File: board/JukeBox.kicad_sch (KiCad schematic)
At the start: 70 parts, among them J1 USB_B_Micro, J2 Conn_01x03, J3 Conn_01x04, J4 Conn_01x08, J5 Conn_01x01, J6 Conn_01x03, J7 Conn_01x03, SW1 SW_SPST, SW10 SW_SPST, SW11 SW_SPST, SW12 SW_SPST, SW2 SW_SPST, SW3 SW_SPST, SW4 SW_SPST, SW5 SW_SPST, SW6 SW_SPST, SW7 SW_SPST, SW8 SW_SPST, SW9 SW_SPST, U1 NCP1117-3.3_SOT223, U2 W25Q128JVS, U3 RP2040, Y1 ABLS-12.000MHZ-B4-T

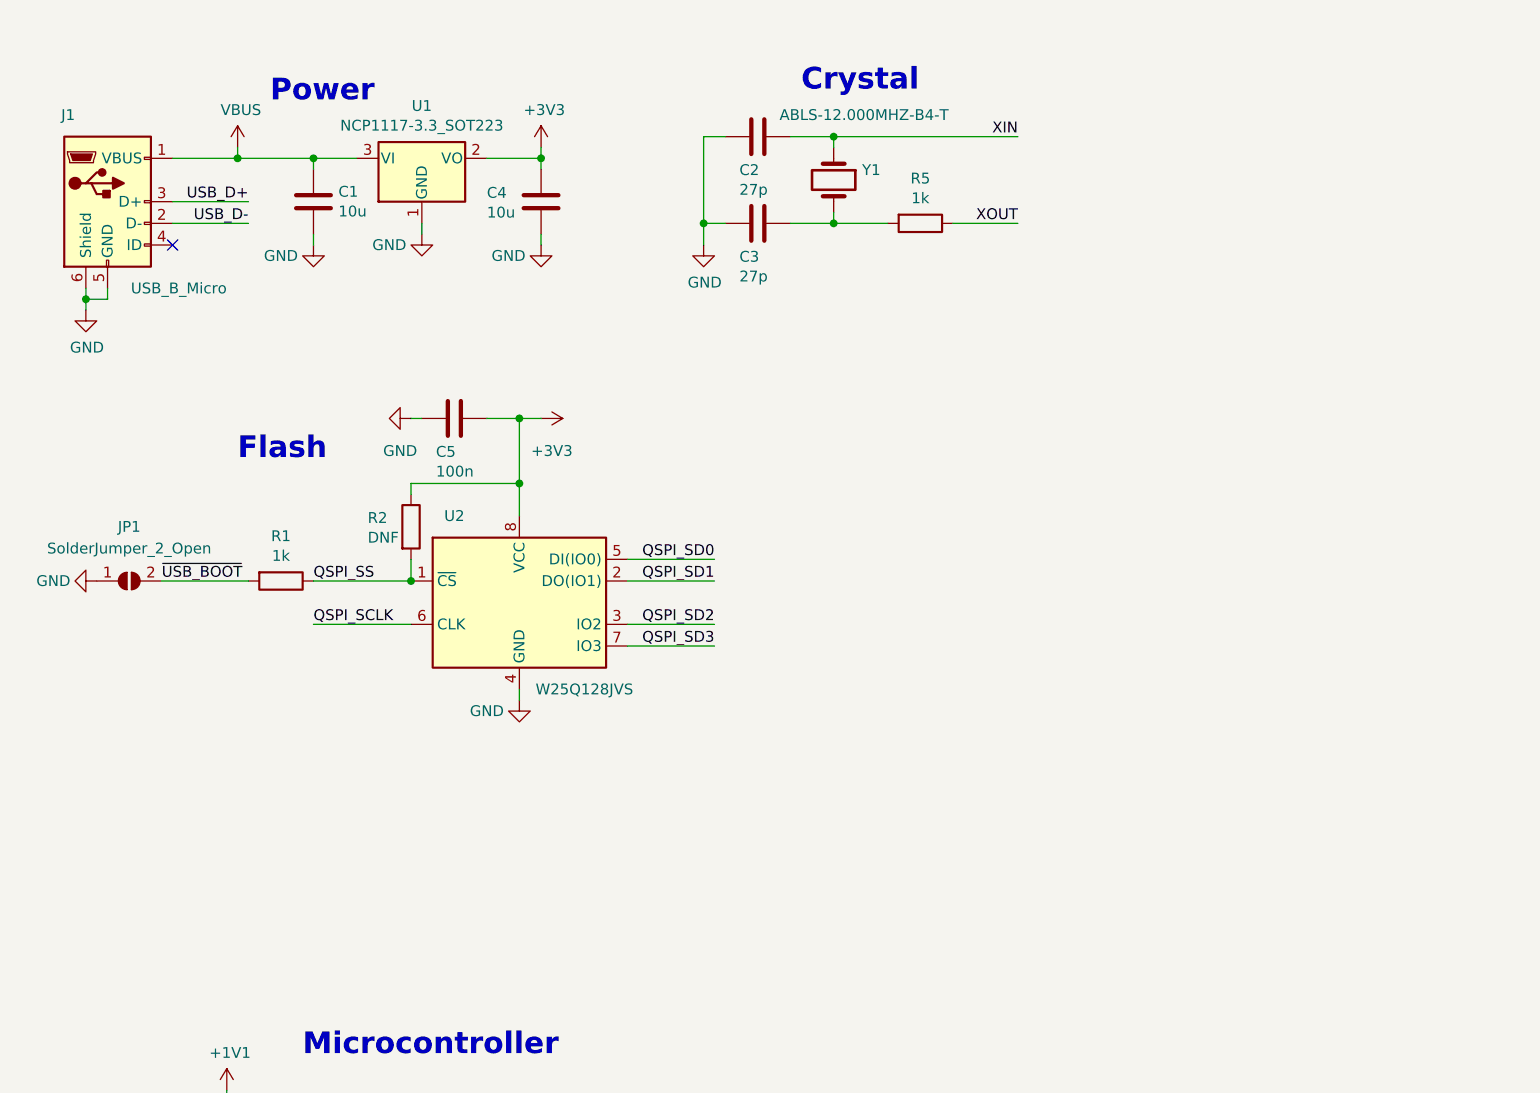
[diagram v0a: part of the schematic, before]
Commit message: add some new footprints and 3d models
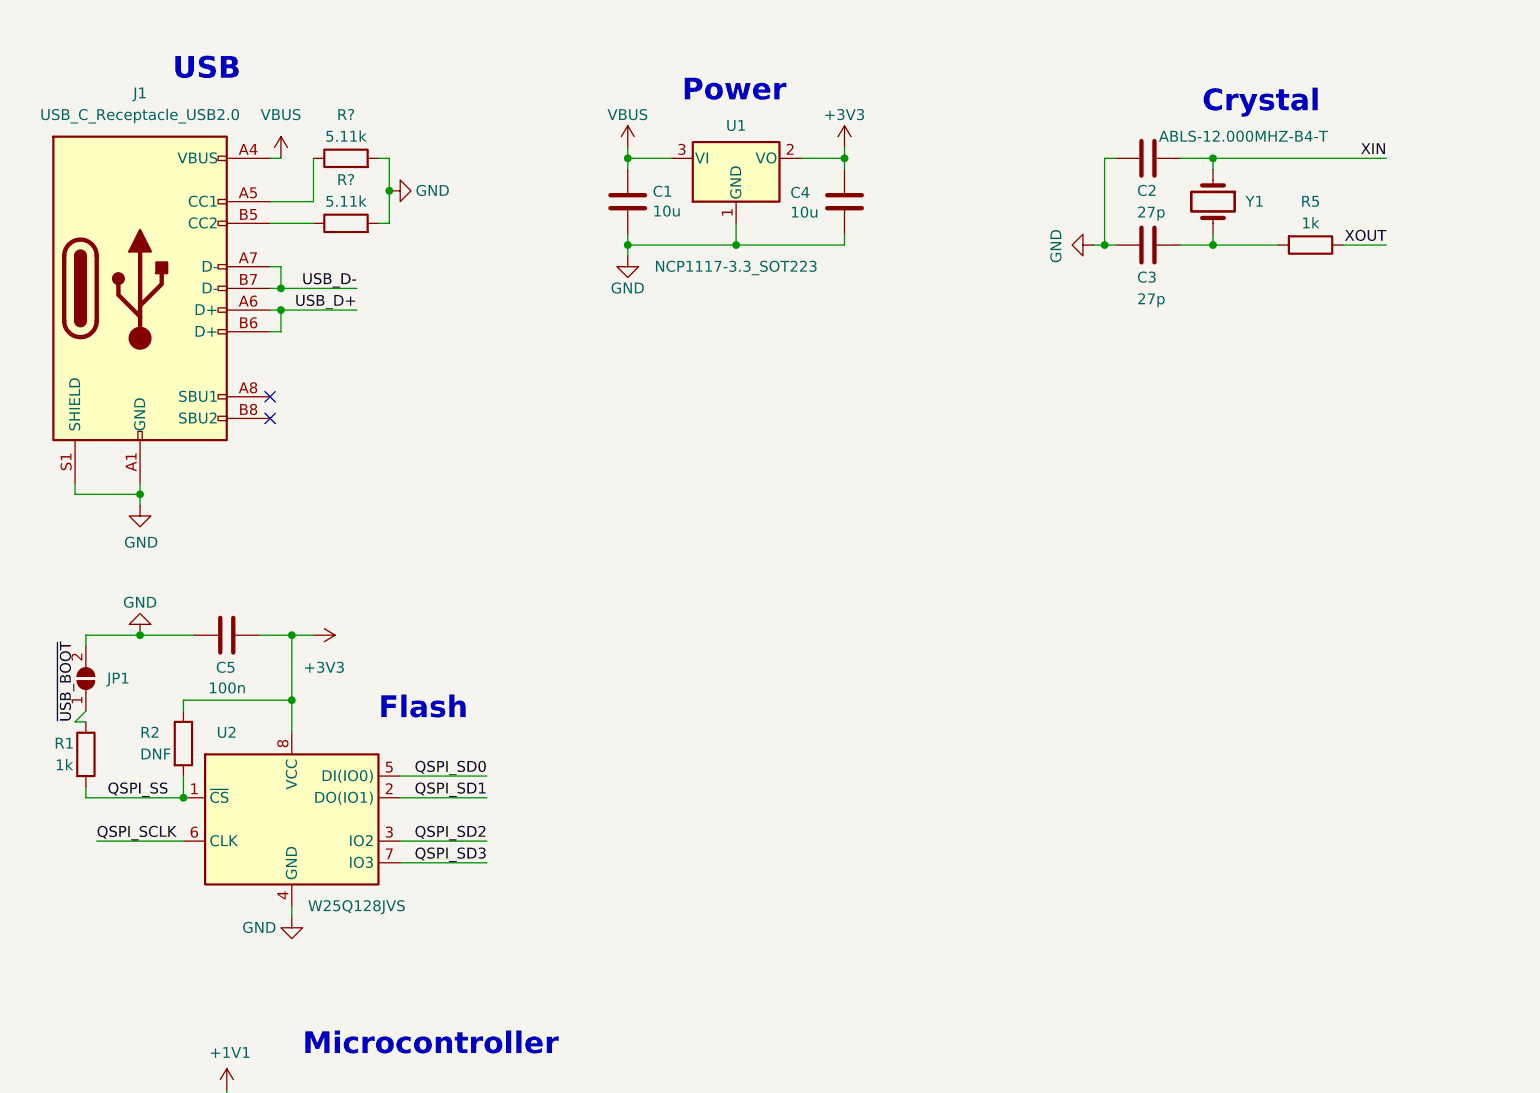
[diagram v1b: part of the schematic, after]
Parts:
- removed J1: USB_B_Micro, RP2040_minimal:USB_Micro-B_Amphenol_10103594-0001LF_Horizontal_modified, symbol Connector:USB_B_Micro
- added J1: USB_C_Receptacle_USB2.0, symbol Connector:USB_C_Receptacle_USB2.0
- added R? (x2): 5.11k, Resistor_SMD:R_1206_3216Metric_Pad1.30x1.75mm_HandSolder, symbol Device:R
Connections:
- net GND: now also JP1.2 (B), J1.A1 (GND), J1.A12 (GND), J1.B1 (GND), J1.B12 (GND), J1.S1 (SHIELD), R?.2, R?.2; no longer JP1.1 (A)
- net QSPI_SS: now also R1.2; no longer R1.1
- net USB_D+: now also J1.A6 (D+), J1.B6 (D+)
- net USB_D-: now also J1.A7 (D-), J1.B7 (D-)
- net VBUS: now also J1.A4 (VBUS), J1.A9 (VBUS), J1.B4 (VBUS), J1.B9 (VBUS)
- net ~{USB_BOOT}: now also JP1.1 (A), R1.1; no longer JP1.2 (B), R1.2
- new net: J1.B5 (CC2), R?.1
- new net: J1.A5 (CC1), R?.1
- no-connect marks 1 -> 2
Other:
- note added: "USB"
- moved on the sheet: C1, C2, C3, C4, C5, JP1, R1, R2, R5, U1, U2, Y1

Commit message: first pass over pcb
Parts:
- C1, C4: footprint Capacitor_SMD:C_0805_2012Metric -> Capacitor_SMD:C_1206_3216Metric_Pad1.33x1.80mm_HandSolder
- C10, C2, C3, C5, C6, C7, C8: footprint Capacitor_SMD:C_0402_1005Metric -> Capacitor_SMD:C_1206_3216Metric_Pad1.33x1.80mm_HandSolder
- J1: footprint (none) -> RP2040_minimal:GCT_USB4085-GF-A_REVA4
- J5: footprint (none) -> Connector_PinHeader_2.54mm:PinHeader_1x01_P2.54mm_Vertical
- JP1: footprint (none) -> Jumper:SolderJumper-2_P1.3mm_Open_RoundedPad1.0x1.5mm
- R1, R2, R3, R4, R5: footprint Capacitor_SMD:C_0402_1005Metric -> Resistor_SMD:R_1206_3216Metric_Pad1.30x1.75mm_HandSolder
- SW1, SW10, SW11, SW12, SW2, SW3, SW4, SW5, SW6, SW7, SW8, SW9: footprint jukebox-footprints:Kailh_PG1350 -> RP2040_minimal:Kailh_Choc_MX_Key
- gave numbers to parts that had none: 2

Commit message: second pass pcb
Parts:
- removed C6, C7: 100n, Capacitor_SMD:C_1206_3216Metric_Pad1.33x1.80mm_HandSolder, symbol Device:C
- added D25, D26, D27, D28, D29, D30: LED, Diode_SMD:D_1206_3216Metric_Pad1.42x1.75mm_HandSolder, symbol Device:LED
- added J8: Conn_01x01, Connector_PinHeader_2.54mm:PinHeader_1x01_P2.54mm_Vertical, symbol Connector_Generic:Conn_01x01
- added R12, R13, R14, R15, R16, R17: 200, Resistor_SMD:R_1206_3216Metric_Pad1.30x1.75mm_HandSolder, symbol Device:R
- renumbered R13 to R10, R14 to R11, R11 to R8, R12 to R9
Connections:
- net GND: now also D25.1 (K), D26.1 (K), D27.1 (K), D28.1 (K), D29.1 (K), D30.1 (K)
- net GPIO10: now also D5.1 (A), D6.1 (A), D7.1 (A), D8.1 (A), J2.2 (Pin_2); no longer J4.5 (Pin_5)
- net GPIO11: now also D10.1 (A), D11.1 (A), D12.1 (A), D9.1 (A), J2.3 (Pin_3); no longer J4.6 (Pin_6)
- net GPIO12: now also J3.1 (Pin_1), R8.2, SW1.2 (B), SW5.2 (B), SW9.2 (B); no longer J4.7 (Pin_7)
- net GPIO13: now also J3.2 (Pin_2), R9.2, SW10.2 (B), SW2.2 (B), SW6.2 (B); no longer J4.8 (Pin_8)
- net GPIO14: now also J3.3 (Pin_3), R10.2, SW11.2 (B), SW3.2 (B), SW7.2 (B)
- net GPIO15: now also J3.4 (Pin_4), R11.2, SW12.2 (B), SW4.2 (B), SW8.2 (B); no longer D13.4 (DIN), J5.1 (Pin_1)
- net GPIO16: no longer D1.1 (A), D2.1 (A), D3.1 (A), D4.1 (A), J2.1 (Pin_1)
- net GPIO17: no longer D5.1 (A), D6.1 (A), D7.1 (A), D8.1 (A), J2.2 (Pin_2)
- net GPIO18: no longer D10.1 (A), D11.1 (A), D12.1 (A), D9.1 (A), J2.3 (Pin_3)
- net GPIO19: no longer J3.1 (Pin_1), R8.2, SW1.2 (B), SW5.2 (B), SW9.2 (B)
- net GPIO2: now also D13.4 (DIN), J5.1 (Pin_1)
- net GPIO20: now also J4.8 (Pin_8); no longer J3.2 (Pin_2), R9.2, SW10.2 (B), SW2.2 (B), SW6.2 (B)
- net GPIO21: now also J4.7 (Pin_7); no longer J3.3 (Pin_3), R10.2, SW11.2 (B), SW3.2 (B), SW7.2 (B)
- net GPIO22: now also J4.6 (Pin_6); no longer J3.4 (Pin_4), R11.2, SW12.2 (B), SW4.2 (B), SW8.2 (B)
- net GPIO23: now also J4.5 (Pin_5)
- net GPIO24: now also J4.4 (Pin_4)
- net GPIO25: now also J4.3 (Pin_3)
- net GPIO3: now also R12.1
- net GPIO4: now also R13.1
- net GPIO5: now also R14.1
- net GPIO6: now also R15.1
- net GPIO7: now also R16.1
- net GPIO8: now also R17.1; no longer J4.3 (Pin_3)
- net GPIO9: now also D1.1 (A), D2.1 (A), D3.1 (A), D4.1 (A), J2.1 (Pin_1); no longer J4.4 (Pin_4)
- net USB_R_D-: now reaches R4.2, U3.46 (USB_DM)
- net USB_R_D+: now reaches R3.2, U3.47 (USB_DP)
- net RGBDOUT: now reaches D24.2 (DOUT)
- net RGBDOUT: now also J8.1 (Pin_1)
- new net: D28.2 (A), R15.2
- new net: D29.2 (A), R16.2
- new net: D26.2 (A), R13.2
- new net: D27.2 (A), R14.2
- new net: D30.2 (A), R17.2
- new net: D25.2 (A), R12.2
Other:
- note added: "Status LEDs"
- moved on the sheet: D13, D14, D15, D16, D17, D18, D19, D20, D21, D22, D23, D24

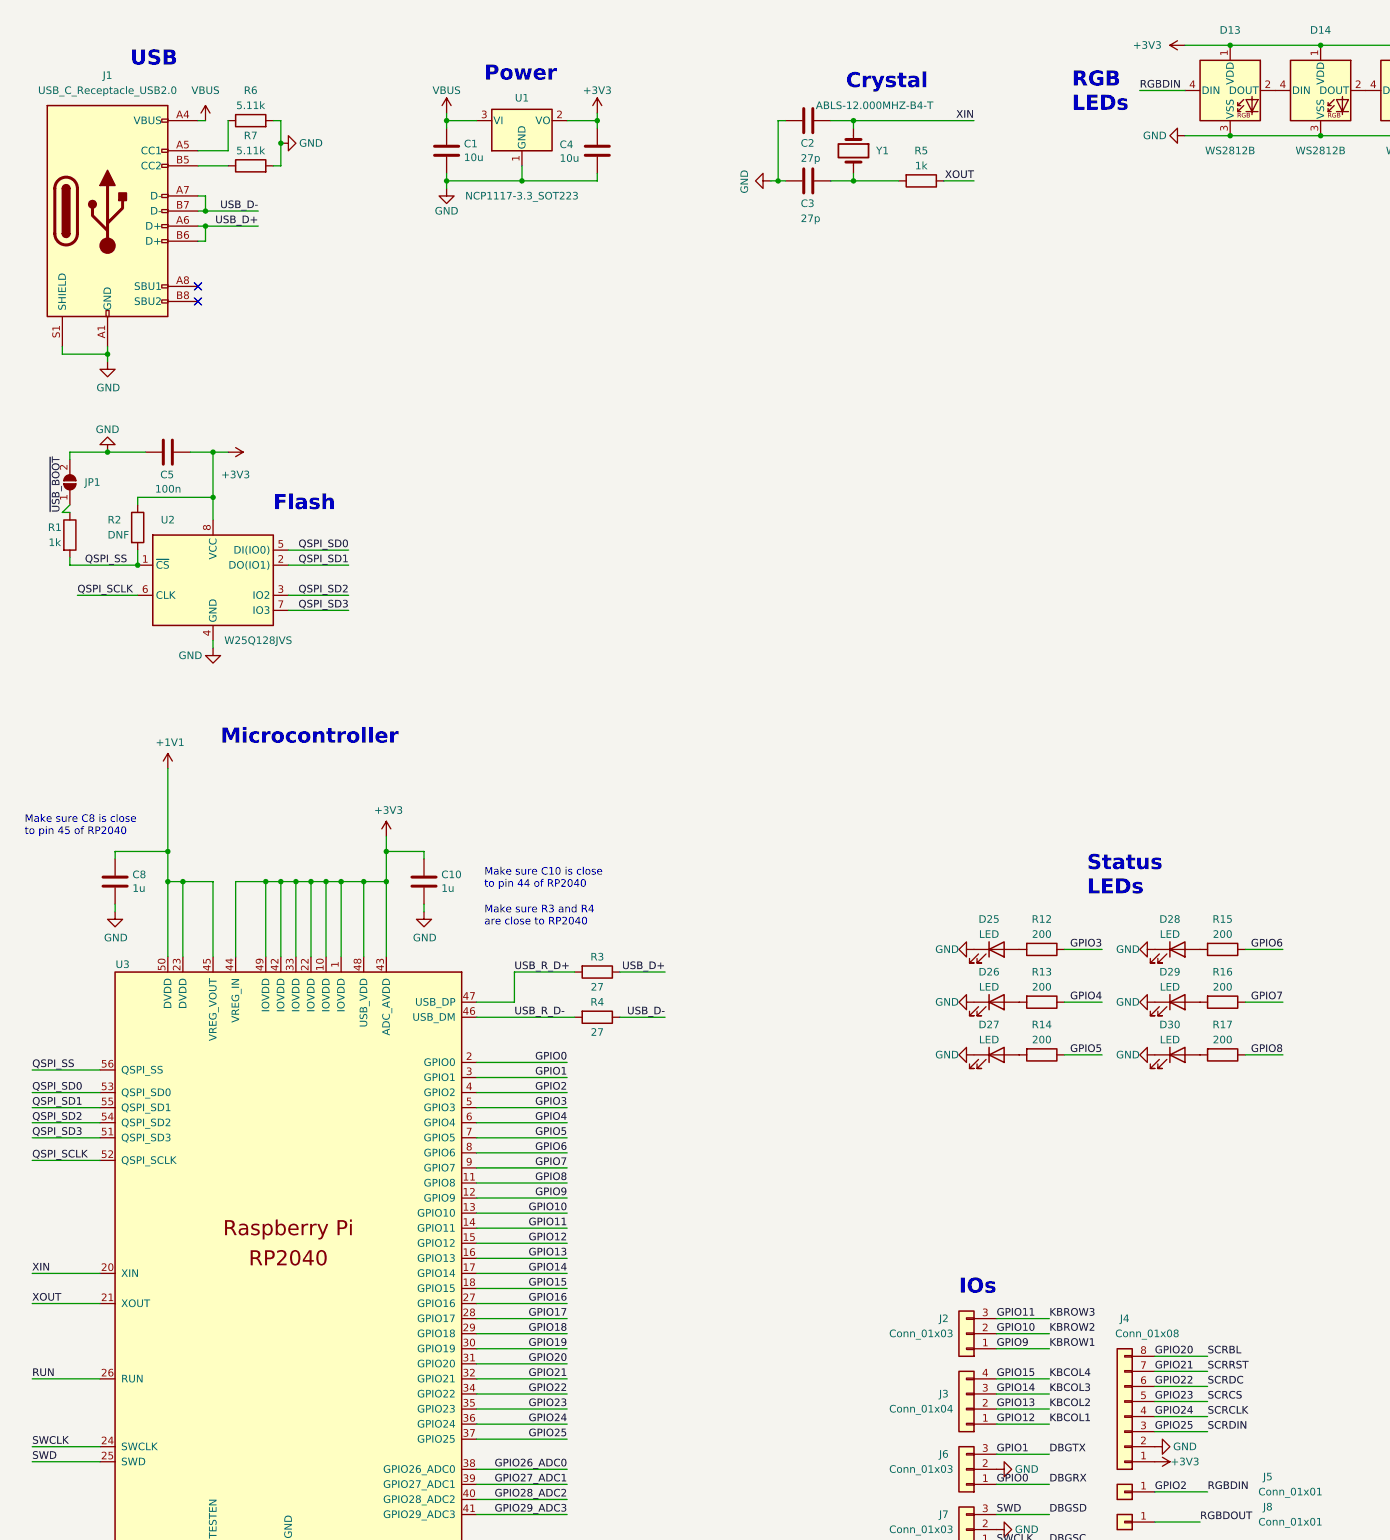
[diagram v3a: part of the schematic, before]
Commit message: move all pcb components to top layer
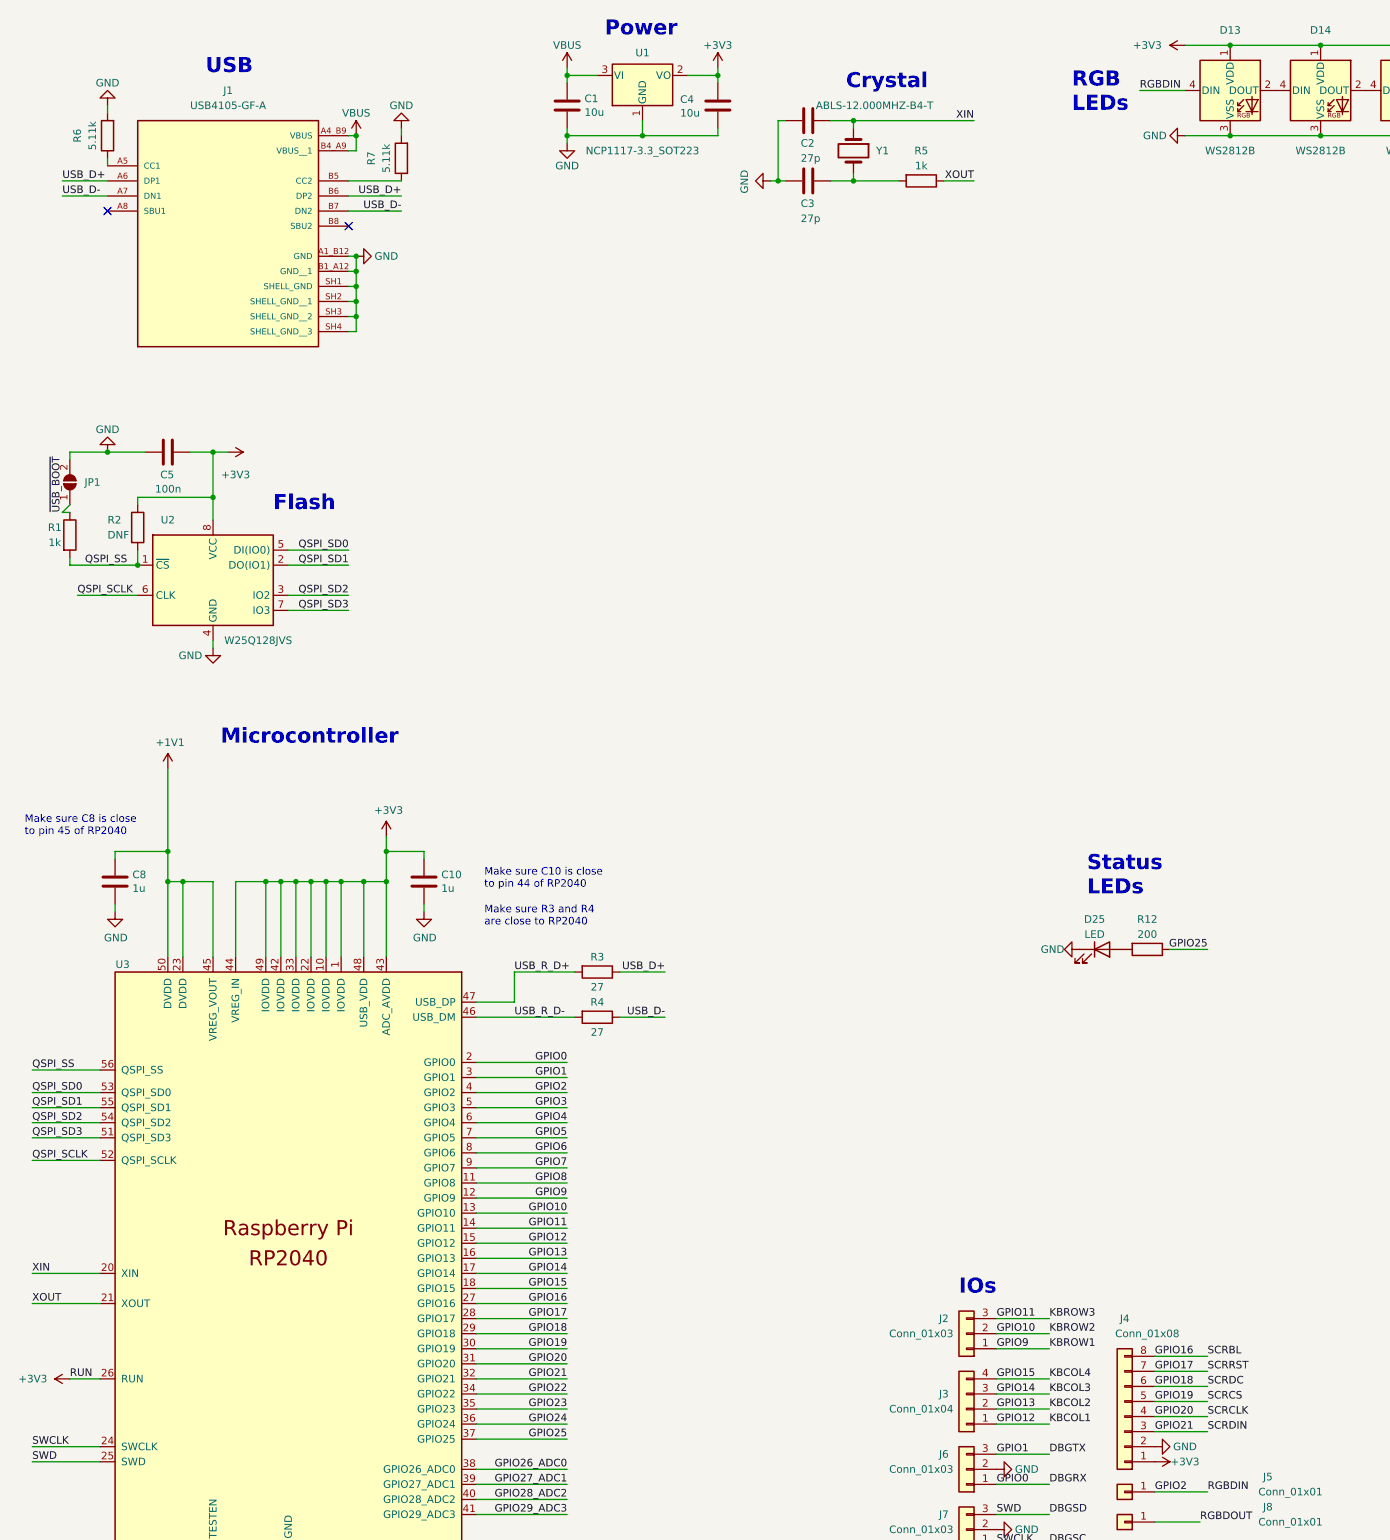
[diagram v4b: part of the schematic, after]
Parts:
- removed D26, D27, D28, D29, D30: LED, Diode_SMD:D_1206_3216Metric_Pad1.42x1.75mm_HandSolder, symbol Device:LED
- removed J1: USB_C_Receptacle_USB2.0, RP2040_minimal:GCT_USB4085-GF-A_REVA4, symbol Connector:USB_C_Receptacle_USB2.0
- removed R13, R14, R15, R16, R17: 200, Resistor_SMD:R_1206_3216Metric_Pad1.30x1.75mm_HandSolder, symbol Device:R
- added J1: USB4105-GF-A, RP2040_minimal:GCT_USB4105-GF-A, symbol USB4105-GF-A:USB4105-GF-A
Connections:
- net RUN is gone; now on net +3V3: U3.26 (RUN)
- net GND: now also J1.A1_B12 (GND), J1.B1_A12 (GND__1), J1.SH1 (SHELL_GND), J1.SH2 (SHELL_GND__1), J1.SH3 (SHELL_GND__2), J1.SH4 (SHELL_GND__3)
- net GPIO16: now also J4.8 (Pin_8)
- net GPIO17: now also J4.7 (Pin_7)
- net GPIO18: now also J4.6 (Pin_6)
- net GPIO19: now also J4.5 (Pin_5)
- net GPIO20: now also J4.4 (Pin_4); no longer J4.8 (Pin_8)
- net GPIO21: now also J4.3 (Pin_3); no longer J4.7 (Pin_7)
- net GPIO22: no longer J4.6 (Pin_6)
- net GPIO23: no longer J4.5 (Pin_5)
- net GPIO24: no longer J4.4 (Pin_4)
- net GPIO25: now also R12.1; no longer J4.3 (Pin_3)
- net GPIO3: no longer R12.1
- net USB_D+: now also J1.A6 (DP1), J1.B6 (DP2)
- net USB_D-: now also J1.A7 (DN1), J1.B7 (DN2)
- net VBUS: now also J1.A4_B9 (VBUS), J1.B4_A9 (VBUS__1)
- net at R7.1: now also J1.B5 (CC2)
- net at R6.1: now also J1.A5 (CC1)
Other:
- moved on the sheet: C1, C4, D25, R12, R6, R7, U1

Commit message: minor adjustments
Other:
- moved on the sheet: C1, C4, U1
